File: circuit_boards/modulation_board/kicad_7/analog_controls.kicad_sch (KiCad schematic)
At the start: 28 parts

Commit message: Progress on circuit boards
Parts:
- added C414: 100n, Capacitor_SMD:C_0603_1608Metric, symbol Device:C
- C401, C402, C403, C404, C405, C406, C407, C408, C409, C410, C411, C412: renamed from C?; footprint (none) -> Capacitor_SMD:C_0603_1608Metric
- C413: renamed from C?; value C -> 100n; footprint (none) -> Capacitor_SMD:C_0603_1608Metric
- R401: renamed from R?; value R -> 5k6; footprint (none) -> Resistor_SMD:R_0603_1608Metric
- R402: renamed from R?; value R -> 10k; footprint (none) -> Resistor_SMD:R_0603_1608Metric
- RV401, RV402, RV403, RV404, RV405, RV406, RV407, RV408, RV412: renamed from RV?; footprint (none) -> Potentiometer_THT:Potentiometer_Alpha_RD901F-40-00D_Single_Vertical
- RV409, RV410, RV411: renamed from RV?; footprint (none) -> custom_footprints:Bourns_PTV09
- gave numbers to parts that had none: 1
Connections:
- net +3.3V: now also C414.1
- net GND: now also C414.2
- net MODOSC_RISE_TIME: now also U5.7 (I2); no longer U5.21 (I10)
- net MOD_ENV_A: now also U5.19 (I12); no longer U5.5 (I4)
- net MOD_ENV_D: now also U5.18 (I13); no longer U5.4 (I5)
- net MOD_ENV_R: now also U5.16 (I15); no longer U5.2 (I7)
- net MOD_ENV_S: now also U5.17 (I14); no longer U5.3 (I6)
- net S_AND_H_GLIDE: now also U5.21 (I10); no longer U5.20 (I11)
- net VCA_ENV_A: now also U5.9 (I0); no longer U5.23 (I8)
- net VCA_ENV_R: now also U5.8 (I1); no longer U5.22 (I9)
- net VCF_ENV_A: now also U5.22 (I9); no longer U5.9 (I0)
- net VCF_ENV_D: now also U5.23 (I8); no longer U5.8 (I1)
- net VCF_ENV_R: now also U5.3 (I6); no longer U5.6 (I3)
- net VCF_ENV_S: now also U5.2 (I7); no longer U5.7 (I2)
- net PORTAMENTO_TIME: now reaches C413.1, R401.2, R402.1
- net PORTAMENTO_TIME: now also U5.20 (I11); no longer U5.19 (I12)
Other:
- moved on the sheet: C413, R401, R402

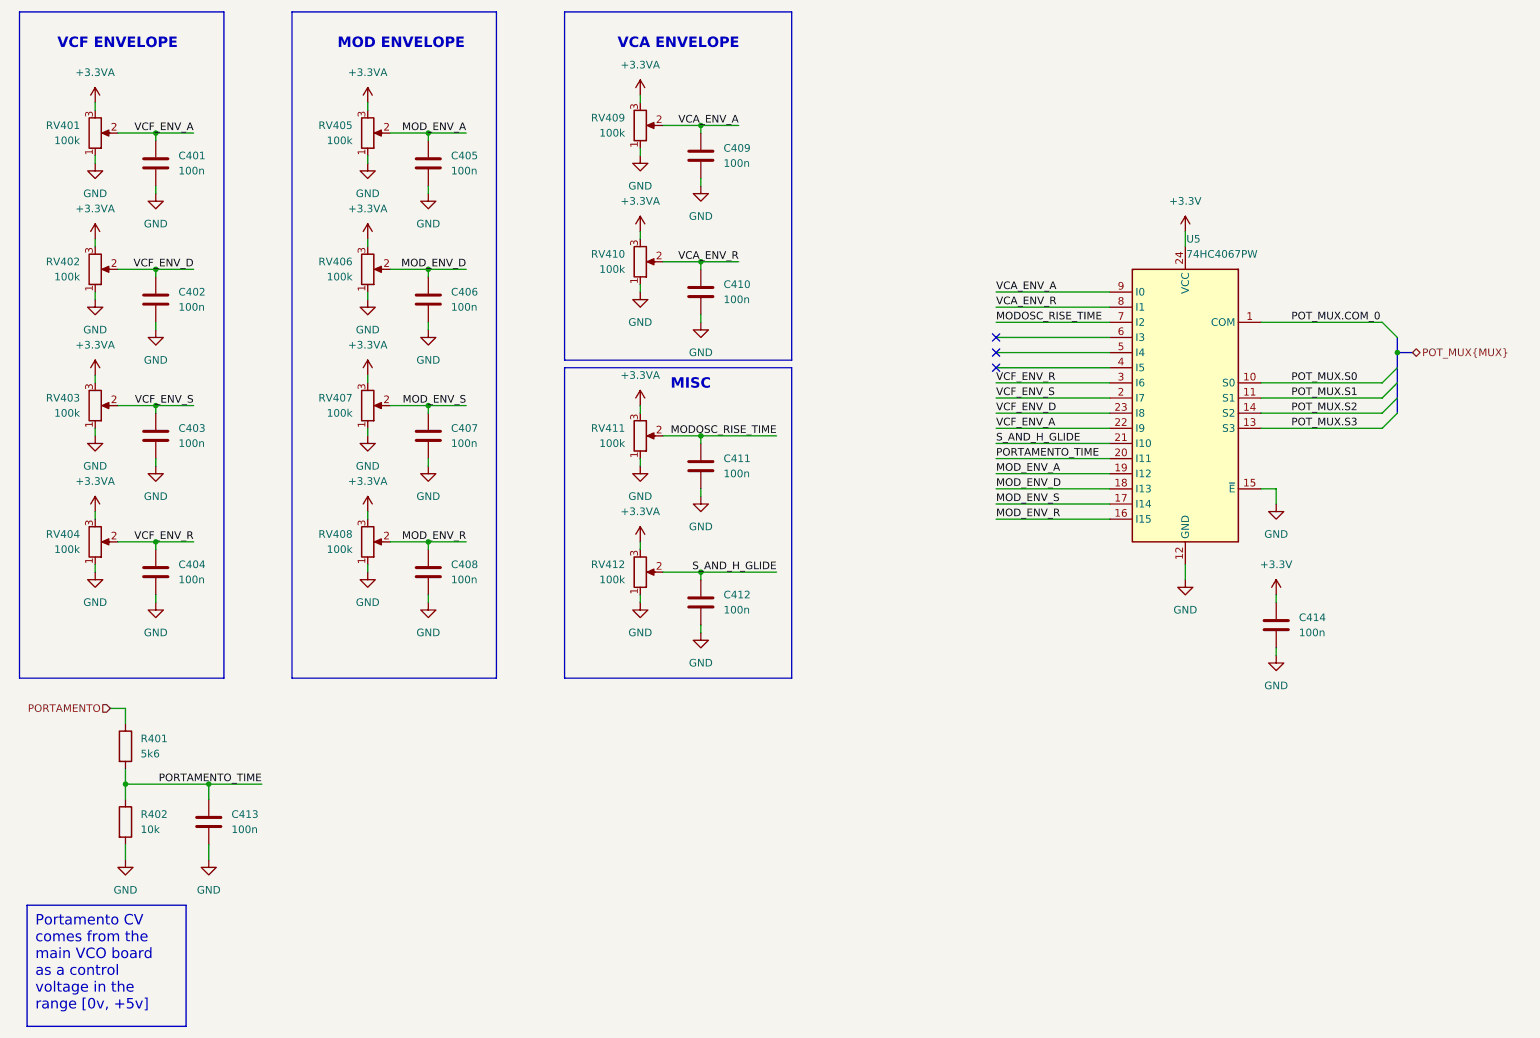
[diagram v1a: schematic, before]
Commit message: Tweaks to mod board, add debug pin
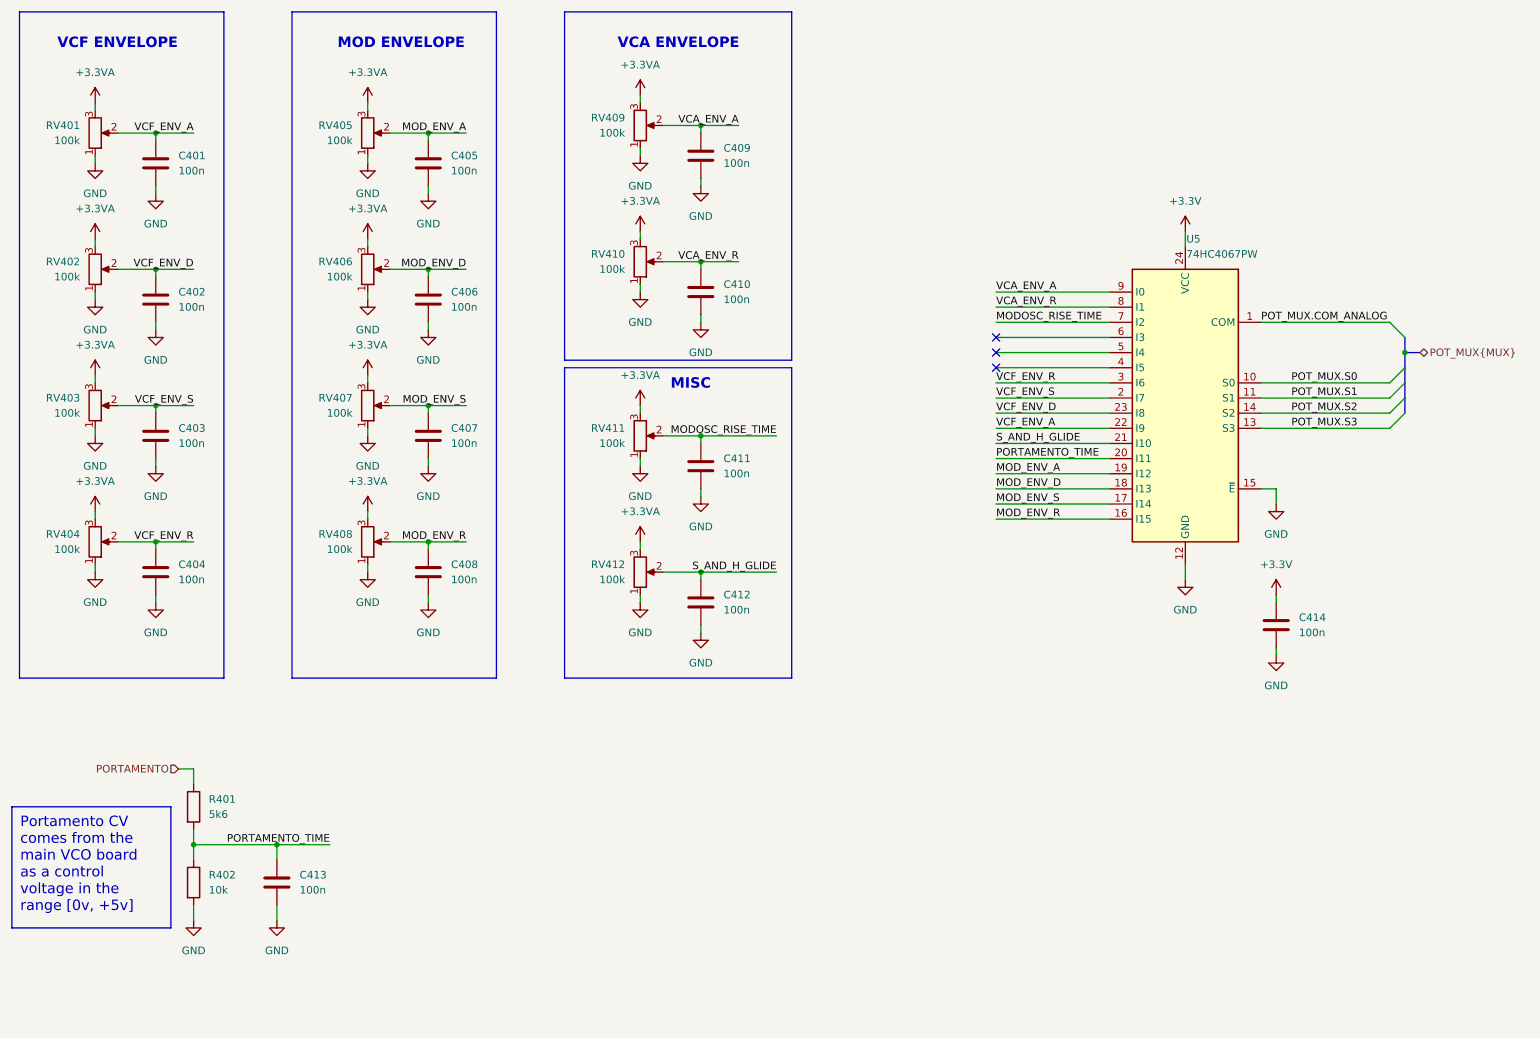
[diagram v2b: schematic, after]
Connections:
- net POT_MUX.COM_0 renamed POT_MUX.COM_ANALOG
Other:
- moved on the sheet: C413, R401, R402
